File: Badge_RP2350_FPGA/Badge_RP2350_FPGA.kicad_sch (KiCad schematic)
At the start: 0 parts

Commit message: add power delivery by Carlo
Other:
- added sheet Power delivery (power_delivery_sch.kicad_sch)
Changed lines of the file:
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@@
+	)
+	(sheet
+		(at 110.49 114.3)
+		(size 77.47 49.53)
+		(exclude_from_sim no)
+		(in_bom yes)
+		(on_board yes)
+		(dnp no)
+		(fields_autoplaced yes)
+		(stroke
+			(width 0.1524)
+			(type solid)
+		)
+		(fill
+			(color 0 0 0 0)
+		)
+		(property "Sheetname" "Power delivery"
+			(at 110.49 113.5884 0)
+			(show_name no)
+			(do_not_autoplace no)
+			(effects
+				(font
+					(size 1.27 1.27)
+				)
+				(justify left bottom)
+			)
+		)
+		(property "Sheetfile" "power_delivery_sch.kicad_sch"
+			(at 110.49 164.4146 0)
+			(show_name no)
+			(do_not_autoplace no)
+			(effects
+				(font
+					(size 1.27 1.27)
+				)
+				(justify left top)
+			)
+		)
+		(instances
+			(project "Badge_RP2350_FPGA"
+				(path "/0ce87b49-0553-4a87-87c1-84e31180901e"
+					(page "5")
+				)
+			)
+		)
 	)
 	(sheet

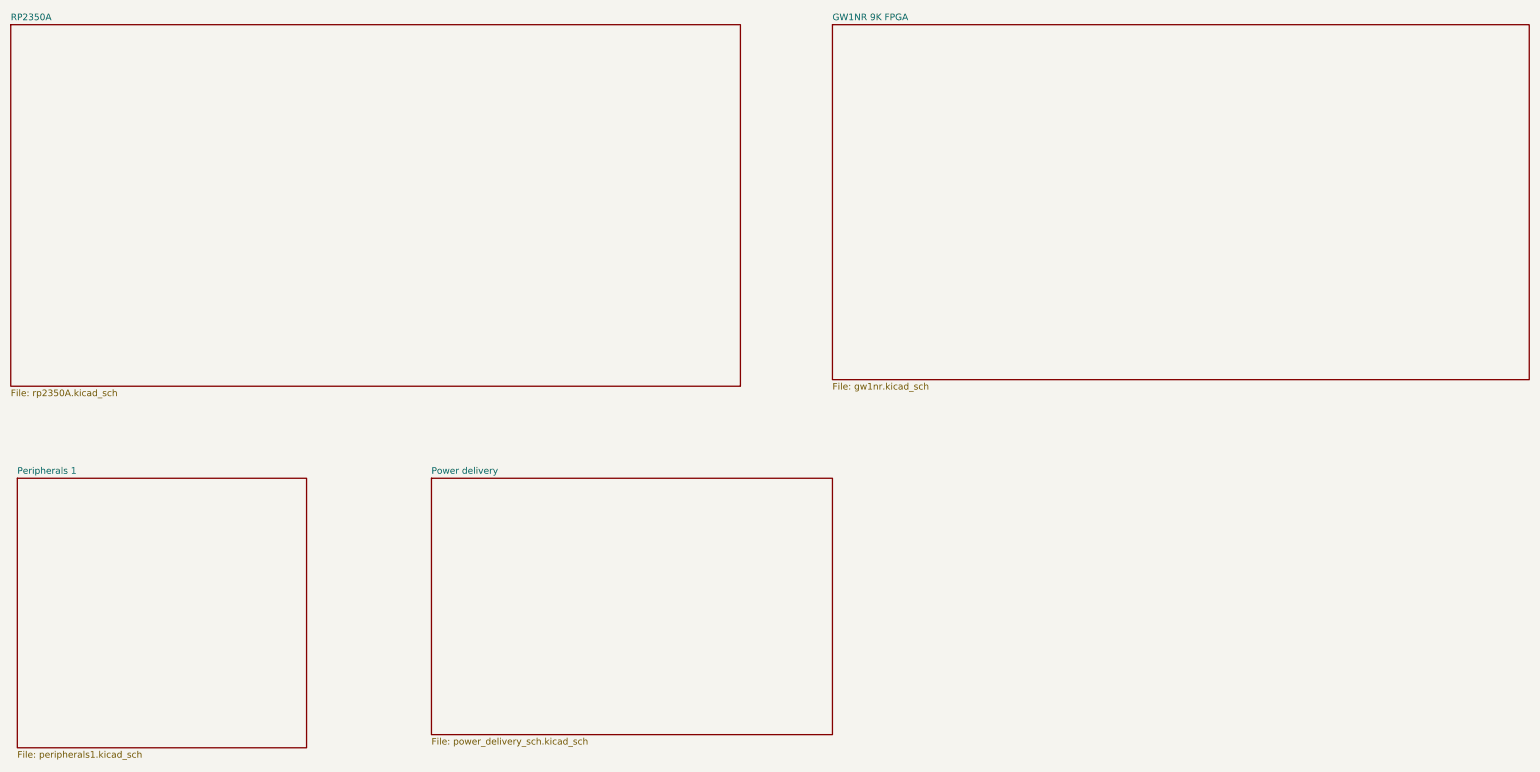
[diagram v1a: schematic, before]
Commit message: add type c port and uart connections
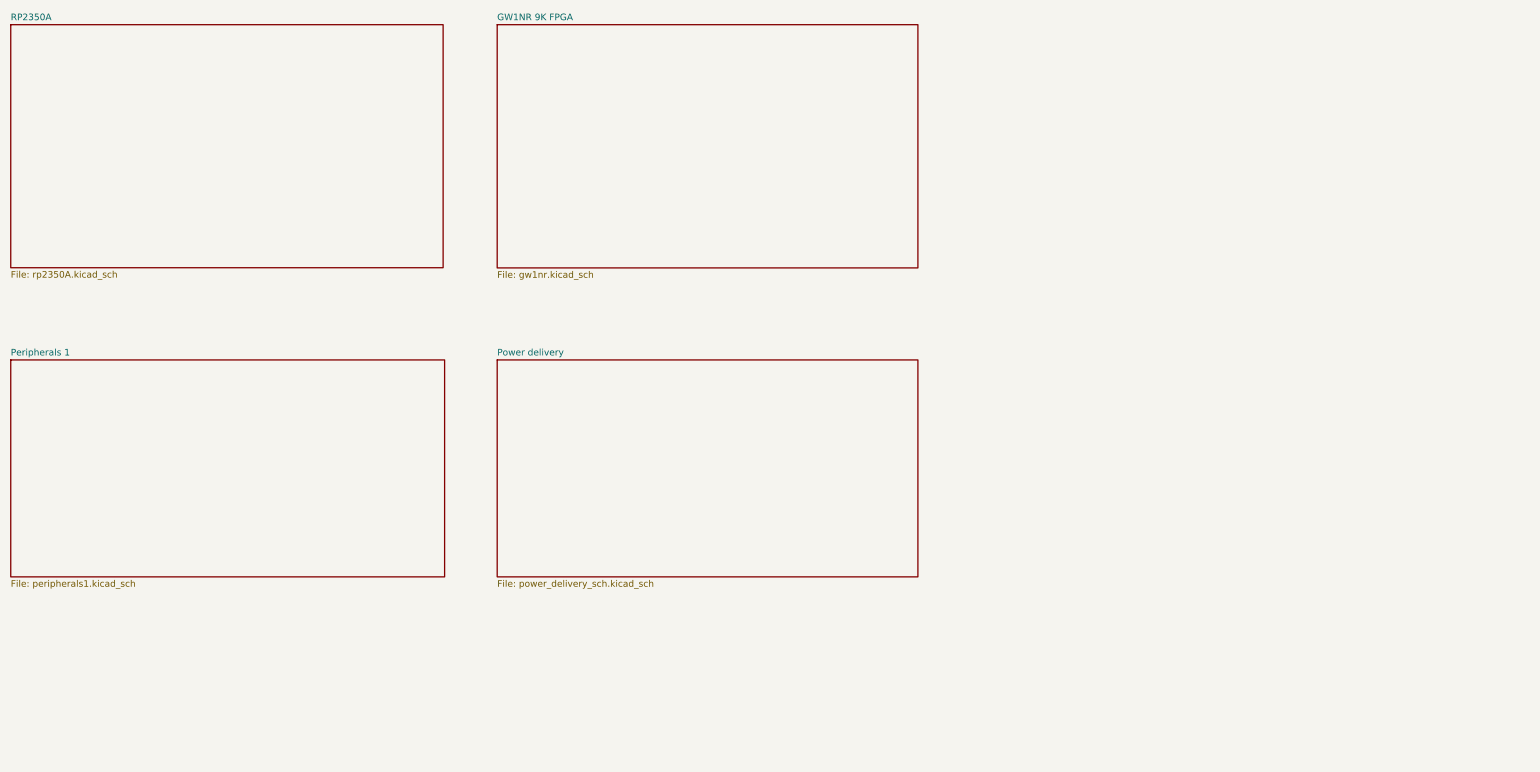
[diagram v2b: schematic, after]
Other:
- company: (none) -> SemiTO-V, RISC-V Student Team
- title: (none) -> RISC-V Summit Europe Badge
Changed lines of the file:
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@@
 	(generator "eeschema")
 	(generator_version "10.0")
-	(paper "A3")
+	(paper "A4")
+	(title_block
+		(title "RISC-V Summit Europe Badge")
+		(date "2026-03-29")
+		(rev "v1.0")
+		(company "SemiTO-V, RISC-V Student Team")
+		(comment 3 "License: CERN-OHL-W")
+		(comment 4 "Authors: Tan Siret Akıncı, Alessandro Bochino, Carlo Bendelli, Arianna Bruno")
+	)
 	(sheet
-		(at 187.96 26.67)
-		(size 134.62 68.58)
+		(at 123.19 26.67)
+		(size 81.28 46.99)
 		(exclude_from_sim no)
 		(in_bom yes)
@@
 		)
 		(property "Sheetname" "GW1NR 9K FPGA"
-			(at 187.96 25.9584 0)
+			(at 123.19 25.9584 0)
 			(show_name no)
 			(do_not_autoplace no)
@@
 		)
 		(property "Sheetfile" "gw1nr.kicad_sch"
-			(at 187.96 95.8346 0)
+			(at 123.19 74.2446 0)
 			(show_name no)
 			(do_not_autoplace no)
@@
 	(sheet
 		(at 29.21 26.67)
-		(size 140.97 69.85)
+		(size 83.5338 46.9543)
 		(exclude_from_sim no)
 		(in_bom yes)
@@
 		)
 		(property "Sheetfile" "rp2350A.kicad_sch"
-			(at 29.21 97.1046 0)
+			(at 29.21 74.2089 0)
 			(show_name no)
 			(do_not_autoplace no)
@@
 	)
 	(sheet
-		(at 110.49 114.3)
-		(size 77.47 49.53)
+		(at 123.19 91.44)
+		(size 81.28 41.91)
 		(exclude_from_sim no)
 		(in_bom yes)
@@
 		)
 		(property "Sheetname" "Power delivery"
-			(at 110.49 113.5884 0)
+			(at 123.19 90.7284 0)
 			(show_name no)
 			(do_not_autoplace no)
@@
 		)
 		(property "Sheetfile" "power_delivery_sch.kicad_sch"
-			(at 110.49 164.4146 0)
+			(at 123.19 133.9346 0)
 			(show_name no)
 			(do_not_autoplace no)
@@
 	)
 	(sheet
-		(at 30.48 114.3)
-		(size 55.88 52.07)
+		(at 29.21 91.44)
+		(size 83.82 41.91)
 		(exclude_from_sim no)
 		(in_bom yes)
@@
 		)
 		(property "Sheetname" "Peripherals 1"
-			(at 30.48 113.5884 0)
+			(at 29.21 90.7284 0)
 			(show_name no)
 			(do_not_autoplace no)
@@
 		)
 		(property "Sheetfile" "peripherals1.kicad_sch"
-			(at 30.48 166.9546 0)
+			(at 29.21 133.9346 0)
 			(show_name no)
 			(do_not_autoplace no)

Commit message: edit schematics visually and edit pcb
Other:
- note added: "Credits"
- note added: "Designed by:"
- note added: "Electronic Badge"
- note added: "For RISC-V Summit Europe 2026 Bologna, Italy"
- note added: "Sheets"
- note added: "Sponsored by:"
